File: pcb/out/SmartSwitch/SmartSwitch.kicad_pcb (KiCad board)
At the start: 2 copper layers, 79.8 x 90 mm, 44 parts, among them J1 12V IN, J2 UART, J3 RJ45-A, J4 RJ45-B, J5 RJ45-C, J6 RJ45-D, SW1 EN, SW2 BOOT, U1 MP1584, U2 AMS1117-3.3, U3 ESP32-WROOM-32, U4 MCP23017, U5 DS18B20

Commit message: Zasady rozmieszczania: I/O na krawedziach, strefa 230V, plyty gora/dol
Wdrozone zasady uzytkownika (pcbforge/layout.py + smart_home_230.py):
- I/O (zlacza) na gornej krawedzi; przekazniki + zaciski 230V w osobnej strefie
  na dolnej krawedzi (izolacja od logiki).
- otwory montazowe i zlacze board-to-board w IDENTYCZNYCH wspolrzednych na obu
  plytkach (wspolna Frame) - skladaja sie 1:1.
- gorna plytka WEZSZA o pasy I/O (Design.outline = srodek) - dostep srubokretem
  do zaciskow dolnej plytki.
- osobna dioda/TVS na kazde I/O (regula DIODE_PER_IO).
- 230V: design.mark_mains() -> klasa 'mains' w DSN (1.5mm sciezki, 2.5mm izolacja);
  regula MAINS_UNMARKED pilnuje oznaczenia kontaktow przekaznikow.
- pasywne od spodu (poprawne warstwy B.* + lustro padow w pcb_writer).
- opisy po polsku na silku (Component.label, Design.notes).

Nowe czesci: przekaznik SPDT (szerokie pady 230V), otwor montazowy M3, blok
relay_driver. Reguly swiadome zlacza B2B (sieci miedzyplytkowe nie flagowane).
9 zasad zapisane trwale w knowledge/kb.json. Flagowiec SmartHome230 (2 plyty):
ERC/DRC/reguly 0/0/0, zwalidowane kiutils. Testy 11/11.

Co-Authored-By: Claude Opus 4.8 (1M context) <noreply@anthropic.com>
Claude-Session: https://claude.ai/code/session_01LNGxtK2Jv1rJLBLPTwFQ9C
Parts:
- added D10: ESD, pcbforge:D_SOD-323, F.Cu at (64.2, 85.1)
- added D11: ESD, pcbforge:D_SOD-323, F.Cu at (69.2, 85.1)
- added D12: ESD, pcbforge:D_SOD-323, F.Cu at (74.3, 85.1)
- added D13: ESD, pcbforge:D_SOD-323, F.Cu at (5.45, 89.0)
- added D14: ESD, pcbforge:D_SOD-323, F.Cu at (10.6, 89.0)
- added D15: ESD, pcbforge:D_SOD-323, F.Cu at (15.7, 89.0)
- added D16: ESD, pcbforge:D_SOD-323, F.Cu at (20.8, 89.0)
- added D17: ESD, pcbforge:D_SOD-323, F.Cu at (25.9, 89.0)
- added D18: ESD, pcbforge:D_SOD-323, F.Cu at (30.9, 89.0)
- added D19: ESD, pcbforge:D_SOD-323, F.Cu at (36.0, 89.0)
- added D8: ESD, pcbforge:D_SOD-323, F.Cu at (54.0, 85.1)
- added D9: ESD, pcbforge:D_SOD-323, F.Cu at (59.0, 85.1)
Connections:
- D5 pad 1: BTN4 -> BTN1
- D6 pad 1: BTN8 -> BTN2
- D7 pad 1: BTN12 -> BTN3
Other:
- board size 79.8 x 90 mm -> 79.8 x 93.8 mm
- board text added: "SmartSwitch"

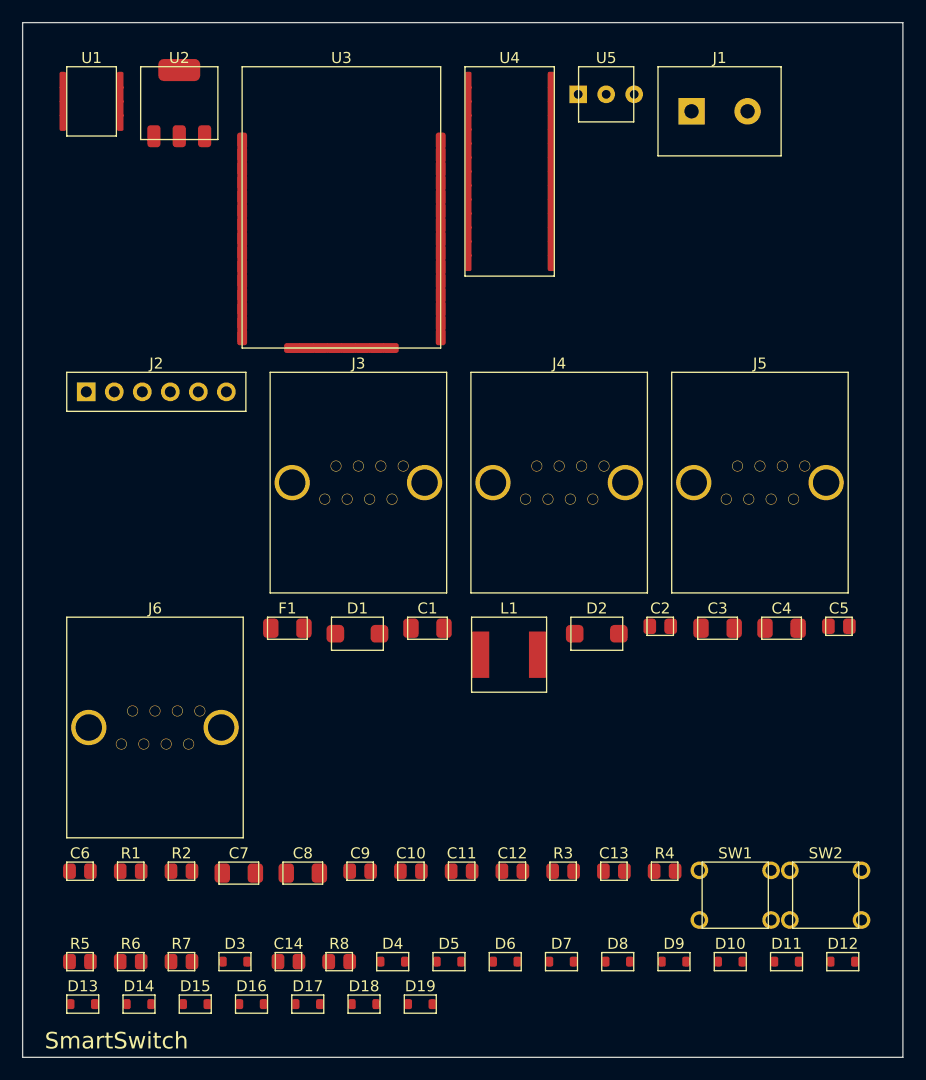
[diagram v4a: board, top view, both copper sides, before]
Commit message: ESP32-S3 + przyciski TFT; kompaktowy layout (szerokosc z liczby zlacz, 2 rzedy)
- Przejscie ESP32-C3 -> ESP32-S3 (duzo GPIO): niezalezne RS485/CAN, dotyk z IRQ,
  4 przyciski nawigacji TFT (GORA/DOL/OK/WSTECZ). Nowa czesc ESP32-S3-WROOM-1.
- Layout: I/O wzdluz krawedzi w 2 rzedach (podwojne w pionie), szerokosc plytki
  wynika z LICZBY zlacz (zmienne szerokosci kolumn) - wejscia na gornej krawedzi,
  wyjscia (zaciski) na dolnej. auto_frame() dobiera ciasna wspolna ramke.
- Przekazniki pakowane w strefe 230V (kilka rzedow) omijajaca otwory.
- HomeCtrlPro: 280x185 -> 168x192 mm, mniej pustego miejsca. Oba 0/0/0.

Testy 12/12, zwalidowane kiutils. Bloki: esp32s3, button.

Co-Authored-By: Claude Opus 4.8 (1M context) <noreply@anthropic.com>
Claude-Session: https://claude.ai/code/session_01LNGxtK2Jv1rJLBLPTwFQ9C
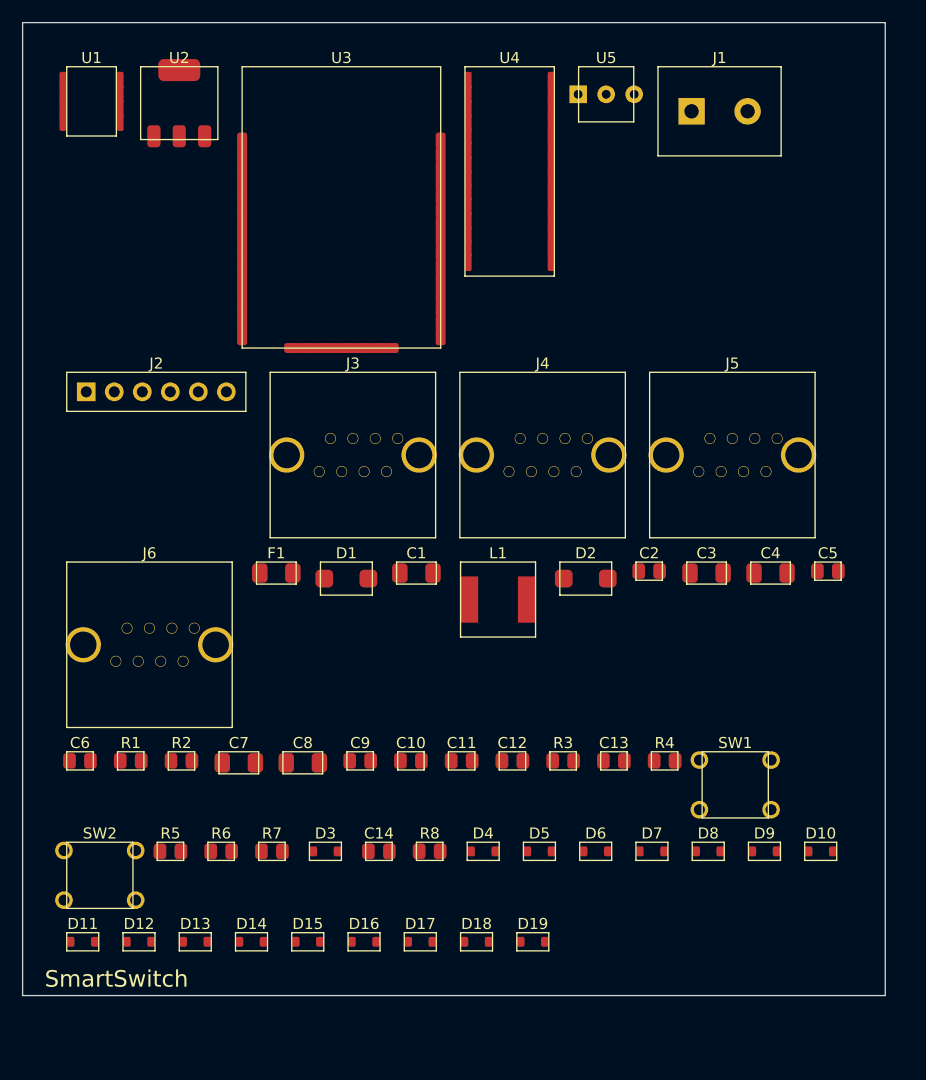
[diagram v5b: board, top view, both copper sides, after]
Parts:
- moved SW2 65.8 mm to (7.00, 77.3)
- moved D11 63.8 mm to (5.45, 83.3)
- moved D12 63.8 mm to (10.6, 83.3)
- moved D4 12.9 mm to (41.8, 75.1)
- moved D5 12.9 mm to (46.9, 75.1)
- moved D6 12.9 mm to (52.0, 75.1)
- moved D9 12.9 mm to (67.2, 75.1)
- moved R7 12.9 mm to (22.6, 75.1)
- moved D3 12.9 mm to (27.4, 75.1)
- moved R5 12.9 mm to (13.4, 75.1)
- moved R6 12.9 mm to (18.0, 75.1)
- moved R8 12.9 mm to (36.9, 75.1)
- moved C14 12.9 mm to (32.3, 75.1)
- moved D7 12.9 mm to (57.0, 75.1)
- moved D8 12.9 mm to (62.1, 75.1)
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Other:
- board size 79.8 x 93.8 mm -> 78.2 x 88.2 mm
